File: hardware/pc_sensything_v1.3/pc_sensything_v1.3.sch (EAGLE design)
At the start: 91 parts, among them IC1 CY8C29666_QFN48, Q1 MBT3904DW1T1, Q2 2.5A/30V, SW2 KMR2, U1 FTS31XS-U, U3 MCP73831, U8 AP2112K-3.3V, Y1 32.768kHz

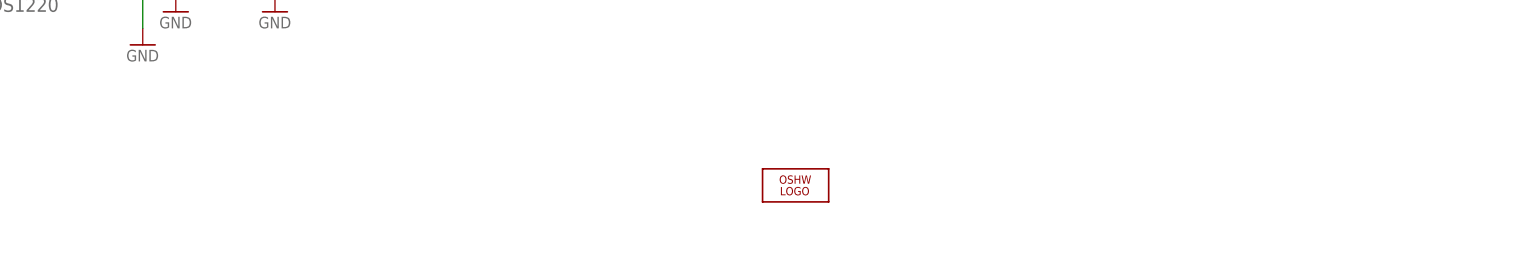
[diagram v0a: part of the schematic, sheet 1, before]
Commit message: Updated Eagle schematic for v1.3 and PDF
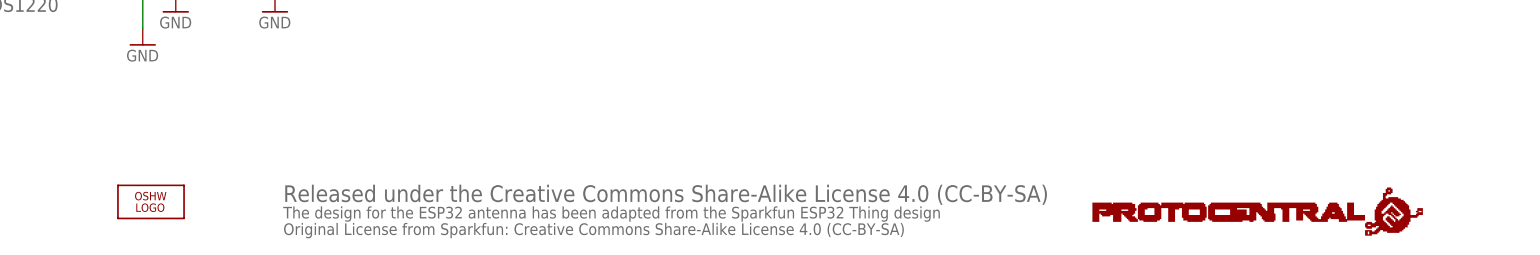
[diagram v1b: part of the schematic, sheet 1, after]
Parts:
- added U$19, U$21: PROTY_LOGO_WITH_TEXT, circuitects:PROTY_LOGO_WITH_TEXT
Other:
- note added: "Original License from Sparkfun: Creative Commons Share-Alike License 4.0 (CC-BY-SA)"
- note added: "Released under the Creative Commons Share-Alike License 4.0 (CC-BY-SA)"
- note added: "The design for the ESP32 antenna has been adapted from the Sparkfun ESP32 Thing design"
- note removed: "CS-----------------IO17"
- note removed: "DRDY-----------IO16"
- note removed: "FDC_SCL------IO12"
- note removed: "FDC_SDA------IO5"
- note removed: "SCL--------------IO2"
- note removed: "SCL_1-----------IO34"
- note removed: "SDA--------------IO15"
- note removed: "SDA_1-----------IO35"
- note removed: "old connection"
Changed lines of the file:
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@@
 <part name="SUPPLY6" library="SparkFun-Aesthetics" deviceset="3.3V" device=""/>
 <part name="P+4" library="supply1" deviceset="+5V" device=""/>
+<part name="U$19" library="circuitects" deviceset="PROTY_LOGO_WITH_TEXT" device=""/>
+<part name="U$21" library="circuitects" deviceset="PROTY_LOGO_WITH_TEXT" device=""/>
 </parts>
 <sheets>
@@
 <text x="330.2" y="180.34" size="1.778" layer="97" font="vector" align="top-center">If DTR is LOW, toggling RTS from HIGH to LOW resets to run mode.
 If RTS is HIGH, toggling DTR from LOW to HIGH resets to bootloader.</text>
-<wire x1="7.62" y1="58.42" x2="83.82" y2="58.42" width="0.1524" layer="101"/>
-<wire x1="83.82" y1="58.42" x2="83.82" y2="2.54" width="0.1524" layer="101"/>
-<text x="12.7" y="50.8" size="1.778" layer="101">DRDY-----------IO16</text>
-<text x="35.56" y="55.88" size="1.778" layer="101">old connection</text>
-<text x="12.7" y="48.26" size="1.778" layer="101">CS-----------------IO17</text>
-<text x="12.7" y="45.72" size="1.778" layer="101">FDC_SCL------IO12</text>
 <wire x1="180.34" y1="256.54" x2="177.8" y2="256.54" width="0.1524" layer="101" style="shortdash"/>
 <wire x1="177.8" y1="256.54" x2="177.8" y2="218.44" width="0.1524" layer="101" style="shortdash"/>
@@
 <text x="213.36" y="233.68" size="1.778" layer="101" rot="R90">VDD3P3_CPU</text>
 <text x="236.22" y="233.68" size="1.778" layer="101" rot="R90">VDD3P3_RTC</text>
-<text x="12.7" y="43.18" size="1.778" layer="101">FDC_SDA------IO5</text>
-<text x="12.7" y="40.64" size="1.778" layer="101">SDA--------------IO15</text>
-<text x="12.7" y="38.1" size="1.778" layer="101">SCL--------------IO2</text>
-<text x="12.7" y="35.56" size="1.778" layer="101">SCL_1-----------IO34</text>
-<text x="12.7" y="33.02" size="1.778" layer="101">SDA_1-----------IO35</text>
+<text x="165.1" y="12.7" size="1.778" layer="95">The design for the ESP32 antenna has been adapted from the Sparkfun ESP32 Thing design</text>
+<text x="165.1" y="10.16" size="1.778" layer="95">Original License from Sparkfun: Creative Commons Share-Alike License 4.0 (CC-BY-SA)</text>
+<text x="165.1" y="15.24" size="2.54" layer="95">Released under the Creative Commons Share-Alike License 4.0 (CC-BY-SA)</text>
 </plain>
 <instances>
@@
 <instance part="GND69" gate="1" x="306.07" y="106.68"/>
 <instance part="JP7" gate="G$1" x="270.51" y="132.08" rot="MR0"/>
-<instance part="LOGO3" gate="G$1" x="243.84" y="17.78"/>
+<instance part="LOGO3" gate="G$1" x="144.78" y="15.24"/>
 <instance part="U$23" gate="VBAT" x="246.38" y="226.06"/>
 <instance part="R25" gate="G$1" x="246.38" y="215.9" rot="R90"/>
@@
 <instance part="SUPPLY6" gate="G$1" x="95.25" y="185.42"/>
 <instance part="P+4" gate="1" x="97.79" y="187.96"/>
+<instance part="U$19" gate="G$1" x="289.56" y="10.16"/>
 </instances>
 <busses>
@@
 <plain>
 <text x="255.27" y="151.13" size="1.778" layer="106">POWER SUPPLY +5V</text>
+<text x="96.52" y="12.7" size="1.778" layer="95">The design for the ESP32 antenna has been adapted from the Sparkfun ESP32 Thing design</text>
+<text x="96.52" y="10.16" size="1.778" layer="95">Original License from Sparkfun: Creative Commons Share-Alike License 4.0 (CC-BY-SA)</text>
+<text x="96.52" y="15.24" size="2.54" layer="95">Released under the Creative Commons Share-Alike License 4.0 (CC-BY-SA)</text>
 </plain>
 <instances>
@@
 <instance part="GND2" gate="1" x="163.83" y="172.72"/>
 <instance part="R24" gate="G$1" x="289.56" y="182.88" rot="R270"/>
+<instance part="U$21" gate="G$1" x="223.52" y="10.16"/>
 </instances>
 <busses>
